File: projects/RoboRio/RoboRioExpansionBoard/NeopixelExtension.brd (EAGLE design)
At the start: 34.2 x 12.7 mm, 6 parts, among them J1 POWER, P1 Input, U1 74AHCT1G08

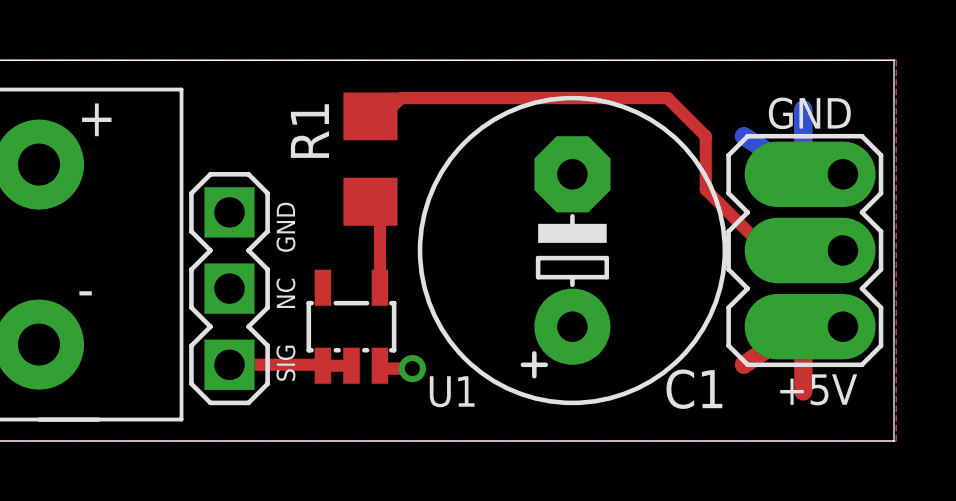
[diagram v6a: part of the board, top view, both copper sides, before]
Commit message: Updated neopixel brd file with team name/number
also fixed a few small routing errors. I believe it is finished now.
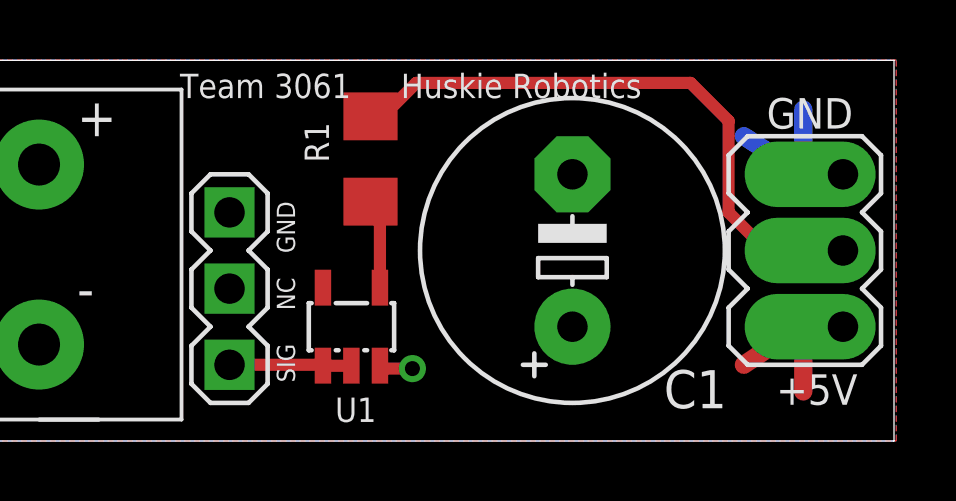
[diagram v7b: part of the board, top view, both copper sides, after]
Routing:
- net N$1: track 19.7 -> 20.9 mm
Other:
- board text added: "Huskie Robotics"
- board text added: "Team 3061"
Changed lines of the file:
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@@
 <text x="13.6398" y="3.2385" size="0.6096" layer="25" rot="R270">SIG</text>
 <text x="10.3505" y="11.303" size="1.778" layer="27" rot="R270">+</text>
+<text x="10.414" y="11.43" size="0.8128" layer="21">Team 3061</text>
+<text x="17.78" y="11.43" size="0.8128" layer="21">Huskie Robotics</text>
 </plain>
 <attributes>
@@
 <elements>
 <element name="R1" library="resistor" package="R1206" value="470" x="16.764" y="9.398" smashed="yes" rot="R270">
-<attribute name="NAME" x="15.3797" y="9.2837" size="1.27" layer="25" ratio="10" rot="R90"/>
+<attribute name="NAME" x="15.3797" y="9.2837" size="0.8128" layer="25" ratio="10" rot="R90"/>
 </element>
 <element name="P1" library="con-lstb-modified" package="MA03-1" value="Input" x="12.065" y="5.08" smashed="yes" rot="R270">
@@
 <element name="U$2" library="NeopixelConnector" package="NEODIRECTSOLDERORMA03-1" value="NEOPIXEL1" x="29.972" y="6.35" smashed="yes" rot="R270"/>
 <element name="U1" library="SOT25" package="SOT25" value="74AHCT1G08" x="16.129" y="3.81" smashed="yes">
-<attribute name="NAME" x="18.6309" y="1.143" size="1.016" layer="25"/>
+<attribute name="NAME" x="15.5829" y="0.635" size="0.8128" layer="25"/>
 </element>
 </elements>
@@
 <contactref element="U$2" pad="DATA"/>
 <wire x1="16.764" y1="10.82" x2="16.764" y2="10.414" width="0.4064" layer="1"/>
-<wire x1="16.764" y1="10.414" x2="17.78" y2="11.43" width="0.4064" layer="1"/>
-<wire x1="17.78" y1="11.43" x2="26.67" y2="11.43" width="0.4064" layer="1"/>
-<wire x1="26.67" y1="11.43" x2="27.94" y2="10.16" width="0.4064" layer="1"/>
-<wire x1="27.94" y1="10.16" x2="27.94" y2="8.382" width="0.4064" layer="1"/>
-<wire x1="27.94" y1="8.382" x2="29.972" y2="6.35" width="0.4064" layer="1"/>
-<wire x1="29.972" y1="6.35" x2="30.48" y2="6.35" width="0.4064" layer="1"/>
-<wire x1="30.48" y1="6.35" x2="32.512" y2="6.35" width="0.4064" layer="1"/>
+<wire x1="16.764" y1="10.414" x2="18.288" y2="11.938" width="0.4064" layer="1"/>
+<wire x1="18.288" y1="11.938" x2="27.432" y2="11.938" width="0.4064" layer="1"/>
+<wire x1="27.432" y1="11.938" x2="28.702" y2="10.668" width="0.4064" layer="1"/>
+<wire x1="28.702" y1="10.668" x2="28.702" y2="7.62" width="0.4064" layer="1"/>
+<wire x1="28.702" y1="7.62" x2="29.972" y2="6.35" width="0.4064" layer="1"/>
+<wire x1="29.972" y1="6.35" x2="32.512" y2="6.35" width="0.4064" layer="1"/>
 </signal>
 <signal name="GND">
 <contactref element="P1" pad="1"/>
 <contactref element="C1" pad="-"/>
-<polygon width="0.6096" layer="16">
+<polygon width="0.6096" layer="16" isolate="0.254">
 <vertex x="34.29" y="12.7"/>
 <vertex x="34.29" y="0"/>
@@
 <wire x1="31.1912" y1="3.8735" x2="29.21" y2="2.54" width="0.6096" layer="1"/>
 <wire x1="31.1912" y1="3.8735" x2="31.1912" y2="1.651" width="0.6096" layer="1"/>
-<polygon width="0.6096" layer="1" spacing="0.6096">
+<polygon width="0.6096" layer="1" spacing="0.6096" isolate="0.254">
 <vertex x="0" y="0"/>
 <vertex x="34.29" y="0"/>
